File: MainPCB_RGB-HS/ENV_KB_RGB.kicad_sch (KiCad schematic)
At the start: 408 parts

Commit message: moved power input for mcu to vsys and also tweaked a bunch of traces to look nicer
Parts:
- C1, C10, C100, C101, C102, C11, C12, C13, C14, C15, C16, C17, C18, C19, C2, C20, C21, C22, C23, C24, C25, C26, C27, C28, C29, C3, C30, C31, C32, C33, C34, C35, C36, C37, C38, C39, C4, C40, C41, C42, C43, C44, C45, C46, C47, C48, C49, C5, C50, C51, C52, C53, C54, C55, C56, C57, C58, C59, C6, C60, C61, C62, C63, C64, C65, C66, C67, C68, C69, C7, C70, C71, C72, C73, C74, C75, C76, C77, C78, C79, C8, C80, C81, C82, C83, C84, C85, C86, C87, C88, C89, C9, C90, C91, C92, C93, C94, C95, C96, C97, C98, C99: value (none) -> 100nF 0603; footprint (none) -> Capacitor_SMD:C_0603_1608Metric
- D0, D1, D10, D11, D12, D13, D14, D15, D16, D17, D18, D19, D2, D20, D21, D22, D23, D24, D25, D26, D27, D28, D29, D3, D30, D31, D32, D33, D34, D35, D36, D37, D38, D39, D4, D40, D41, D42, D43, D44, D45, D46, D47, D48, D49, D5, D50, D51, D52, D53, D54, D55, D56, D57, D58, D59, D6, D60, D61, D62, D63, D64, D65, D66, D67, D68, D69, D7, D70, D71, D72, D73, D74, D75, D76, D77, D78, D79, D8, D80, D81, D82, D83, D84, D85, D86, D87, D88, D9: value (none) -> D; footprint (none) -> EM_Extras:SOD-123+D_DO-35_SOD27_P7.62mm_Horizontal
- H0, H1, H10, H2, H3, H4, H5, H6, H7, H9: value (none) -> MountingHole; footprint (none) -> MountingHole:MountingHole_2.2mm_M2_Pad
- K_0, K_1, K_10, K_11, K_12, K_13, K_14, K_15, K_16, K_17, K_18, K_19, K_2, K_20, K_21, K_22, K_23, K_24, K_25, K_26, K_27, K_28, K_29, K_3, K_30, K_31, K_32, K_33, K_34, K_35, K_36, K_37, K_38, K_39, K_4, K_40, K_41, K_42, K_43, K_44, K_45, K_46, K_47, K_48, K_49, K_5, K_50, K_51, K_52, K_53, K_54, K_55, K_56, K_57, K_58, K_59, K_6, K_60, K_61, K_62, K_63, K_63B1, K_64, K_64B1, K_65, K_66, K_67, K_68, K_69, K_7, K_70, K_71, K_72, K_73, K_74, K_75, K_76, K_77, K_78, K_79, K_8, K_80, K_81, K_82, K_83, K_84, K_85, K_86, K_87, K_88, K_9: value (none) -> KEYSW; footprint (none) -> MX_Only:MXOnly-1U-Hotswap-Modified
- LED1, LED10, LED100, LED101, LED102, LED11, LED12, LED13, LED14, LED15, LED16, LED17, LED18, LED19, LED2, LED20, LED21, LED22, LED23, LED24, LED25, LED26, LED27, LED28, LED29, LED3, LED30, LED31, LED32, LED33, LED34, LED35, LED36, LED37, LED38, LED39, LED4, LED40, LED41, LED42, LED43, LED44, LED45, LED46, LED47, LED48, LED49, LED5, LED50, LED51, LED52, LED53, LED54, LED55, LED56, LED57, LED58, LED59, LED6, LED60, LED61, LED62, LED63, LED64, LED65, LED66, LED67, LED68, LED69, LED7, LED70, LED71, LED72, LED73, LED74, LED75, LED76, LED77, LED78, LED79, LED8, LED80, LED81, LED82, LED83, LED84, LED85, LED86, LED87, LED88, LED89, LED9, LED90, LED91, LED92, LED93, LED94, LED95, LED96, LED97, LED98, LED99: value (none) -> SK6812MINI-E; footprint (none) -> sk6812mini:MX_SK6812MINI-E_REV
- LEDRESISTOR1: value (none) -> 5.1K Resistor 1/4w; footprint (none) -> Resistor_THT:R_Axial_DIN0207_L6.3mm_D2.5mm_P10.16mm_Horizontal
- LEDRESISTOR2: value (none) -> 5.1K Resistor 1/4w; footprint (none) -> Resistor_SMD:R_0805_2012Metric_Pad1.20x1.40mm_HandSolder
- PowerLED0: value (none) -> LED 3MM; footprint (none) -> LED_THT:LED_D3.0mm_FlatTop
- RESISTOR0: value (none) -> 5.1kohm 1/4w; footprint (none) -> Resistor_THT:R_Axial_DIN0207_L6.3mm_D2.5mm_P10.16mm_Horizontal
- RESISTOR1: value (none) -> 5.1kohm 1/4; footprint (none) -> Resistor_THT:R_Axial_DIN0207_L6.3mm_D2.5mm_P10.16mm_Horizontal
- RESISTOR2, RESISTOR3: value (none) -> 5.1kohm 0805; footprint (none) -> Resistor_SMD:R_0805_2012Metric
- RPI0: value (none) -> Pico; footprint (none) -> EM_Extras:RPi_Pico_SMD_TH
- SW-RST0: value (none) -> EVQ; footprint (none) -> Button_Switch_SMD:Panasonic_EVQPUM_EVQPUD
- Stab1: value (none) -> Stabilizer; footprint (none) -> Mounting_Keyboard_Stabilizer:Stabilizer_Cherry_MX_6.25u
- Stab2, Stab3, Stab4: value (none) -> Stabilizer; footprint (none) -> Mounting_Keyboard_Stabilizer:Stabilizer_Cherry_MX_2u
- USB1: value (none) -> TYPE-C-31-M-14; footprint (none) -> josh-connectors:USB_C_TYPE-C-31-M-14
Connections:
- net USBVBUS: now also RPI0.39 (VSYS); no longer RPI0.40 (VBUS)

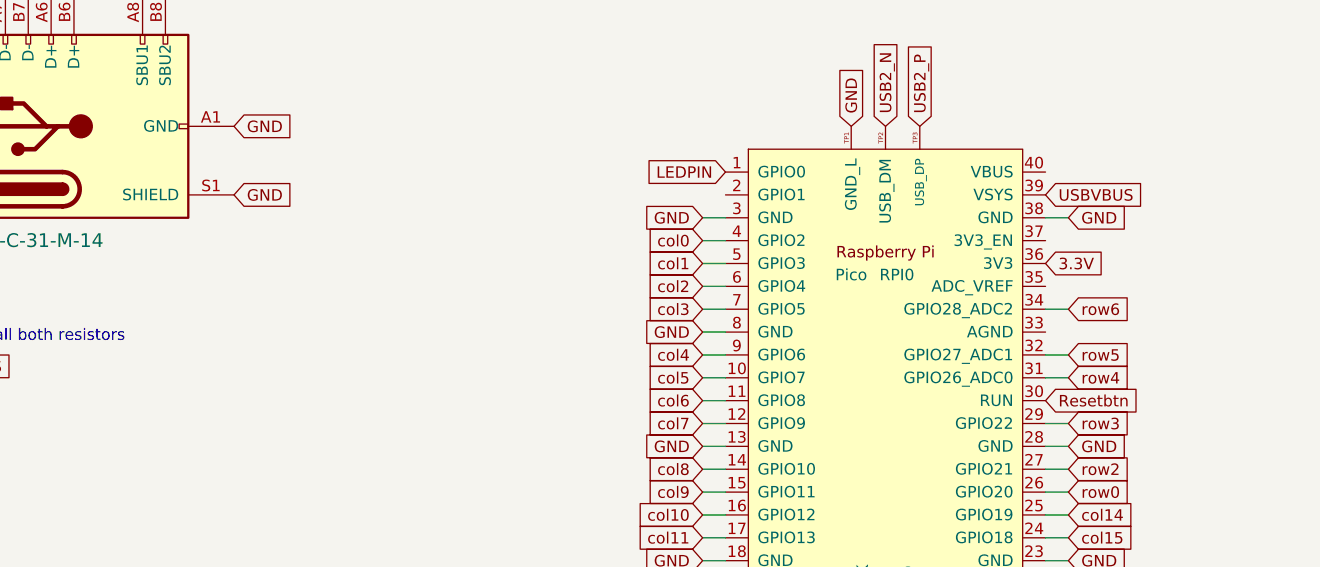
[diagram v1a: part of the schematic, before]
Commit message: Parity changes between RGB and non RGB HS versions
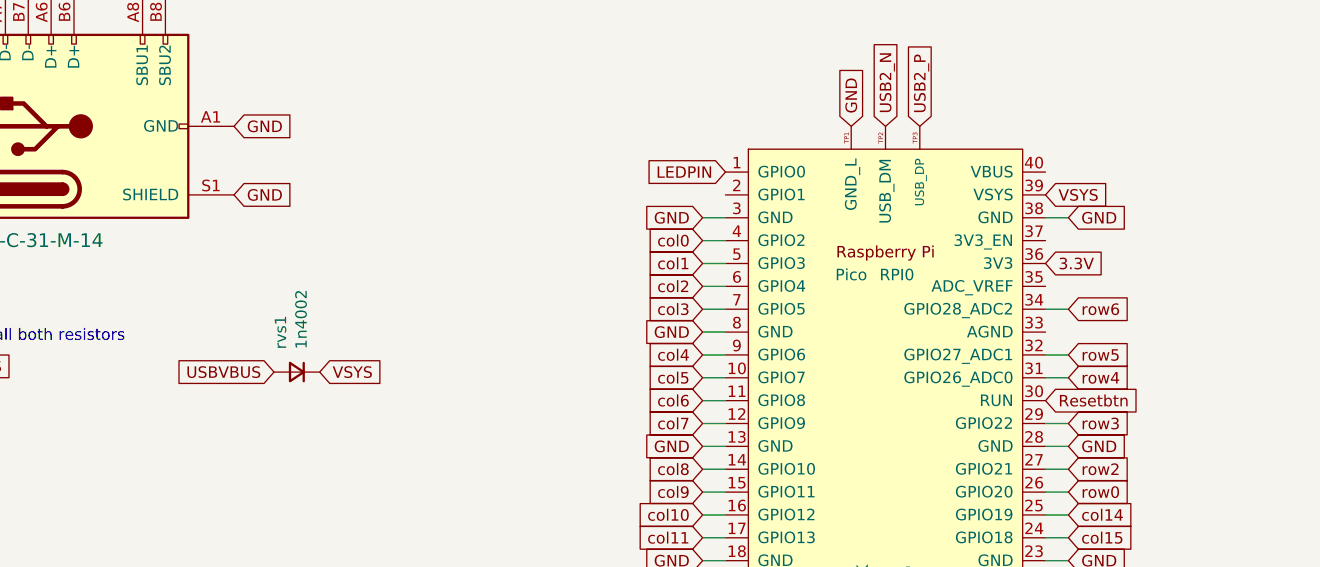
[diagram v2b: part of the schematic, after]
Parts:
- added rvs1: 1n4002, EM_Extras:SOD-123+D_DO-35_SOD27_P7.62mm_Horizontal, symbol Device:D_Small
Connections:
- net USBVBUS: now also rvs1.2 (A); no longer RPI0.39 (VSYS)
- new net VSYS: RPI0.39 (VSYS), rvs1.1 (K)
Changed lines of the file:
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@@
     )
   )
-  (global_label "USBVBUS" (shape input) (at 346.71 233.68 0) (fields_autoplaced)
-    (effects (font (size 1.27 1.27)) (justify left))
-    (property "Intersheet References" "${INTERSHEET_REFS}" (id 0) (at 0 2.54 0)
+  (global_label "USBVBUS" (shape input) (at 260.985 253.365 180) (fields_autoplaced)
+    (effects (font (size 1.27 1.27)) (justify right))
+    (property "Intersheet References" "${INTERSHEET_REFS}" (id 0) (at 607.695 484.505 0)
       (effects (font (size 1.27 1.27)) hide)
     )
@@
     )
   )
+  (global_label "VSYS" (shape input) (at 266.065 253.365 0) (fields_autoplaced)
+    (effects (font (size 1.27 1.27)) (justify left))
+    (property "Intersheet References" "${INTERSHEET_REFS}" (id 0) (at 272.9854 253.2856 0)
+      (effects (font (size 1.27 1.27)) (justify left) hide)
+    )
+  )
   (global_label "col14" (shape input) (at 349.25 269.24 0) (fields_autoplaced)
     (effects (font (size 1.27 1.27)) (justify left))
@@
     )
   )
+  (global_label "VSYS" (shape input) (at 346.71 233.68 0) (fields_autoplaced)
+    (effects (font (size 1.27 1.27)) (justify left))
+    (property "Intersheet References" "${INTERSHEET_REFS}" (id 0) (at 353.6304 233.6006 0)
+      (effects (font (size 1.27 1.27)) (justify left) hide)
+    )
+  )
   (global_label "USBVBUS" (shape input) (at 553.72 102.87 180) (fields_autoplaced)
     (effects (font (size 1.27 1.27)) (justify right))
@@
     (pin "2")
   )
+  (symbol (lib_id "Device:D_Small") (at 263.525 253.365 180) (unit 1)
+    (in_bom yes) (on_board yes)
+    (property "Reference" "rvs1" (id 0) (at 261.747 250.825 90)
+      (effects (font (size 1.27 1.27)) (justify right))
+    )
+    (property "Value" "1n4002" (id 1) (at 264.033 250.825 90)
+      (effects (font (size 1.27 1.27)) (justify right))
+    )
+    (property "Footprint" "EM_Extras:SOD-123+D_DO-35_SOD27_P7.62mm_Horizontal" (id 2) (at 271.145 252.095 0)
+      (effects (font (size 1.27 1.27)) hide)
+    )
+    (property "Datasheet" "" (id 3) (at 271.145 252.095 0)
+      (effects (font (size 1.27 1.27)) hide)
+    )
+    (pin "1")
+    (pin "2")
+  )
   (sheet_instances
     (path "/" (page "1"))
@@
       (reference "USB1") (unit 1) (value "TYPE-C-31-M-14") (footprint "josh-connectors:USB_C_TYPE-C-31-M-14")
     )
+    (path "/fe72a08a-d529-4860-95f3-bd42d36f7bb1"
+      (reference "rvs1") (unit 1) (value "1n4002") (footprint "EM_Extras:SOD-123+D_DO-35_SOD27_P7.62mm_Horizontal")
+    )
   )

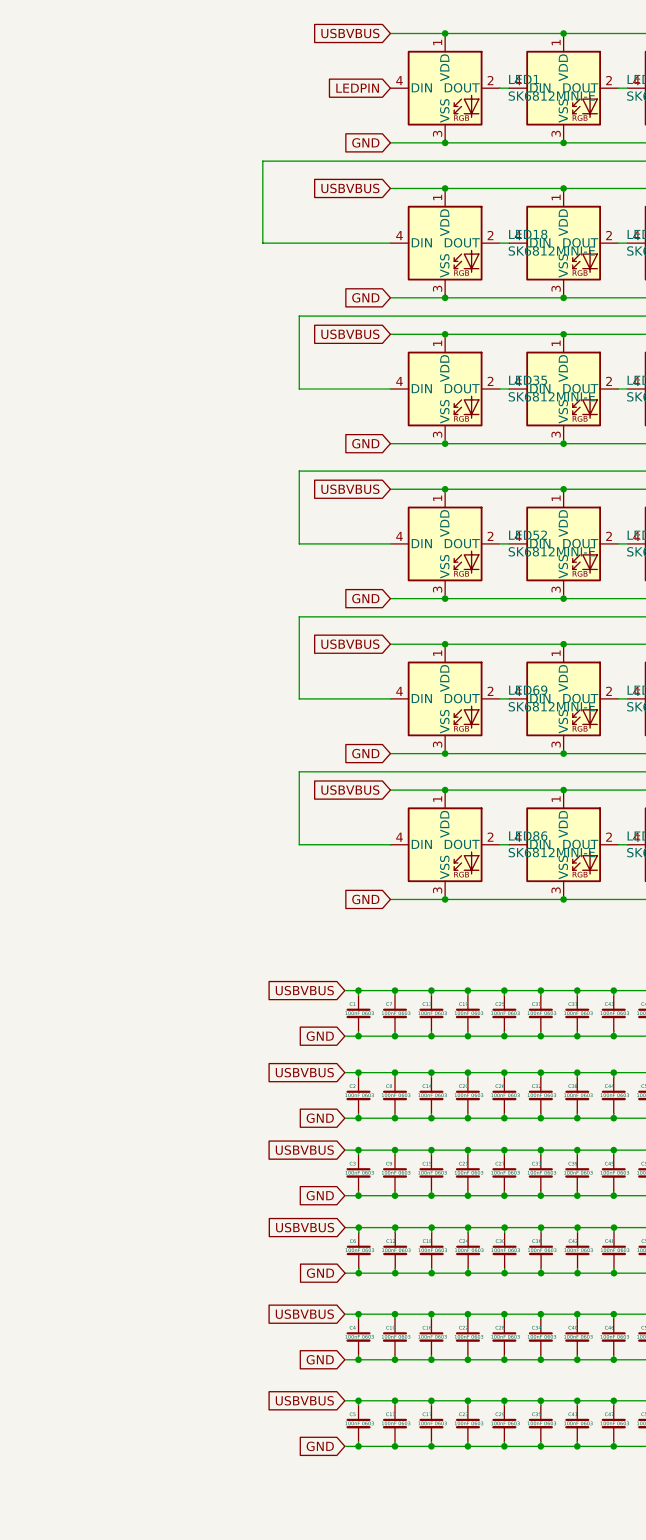
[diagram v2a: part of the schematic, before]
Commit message: Swapped VBUS power to VSYS and fixed edge cut issues.
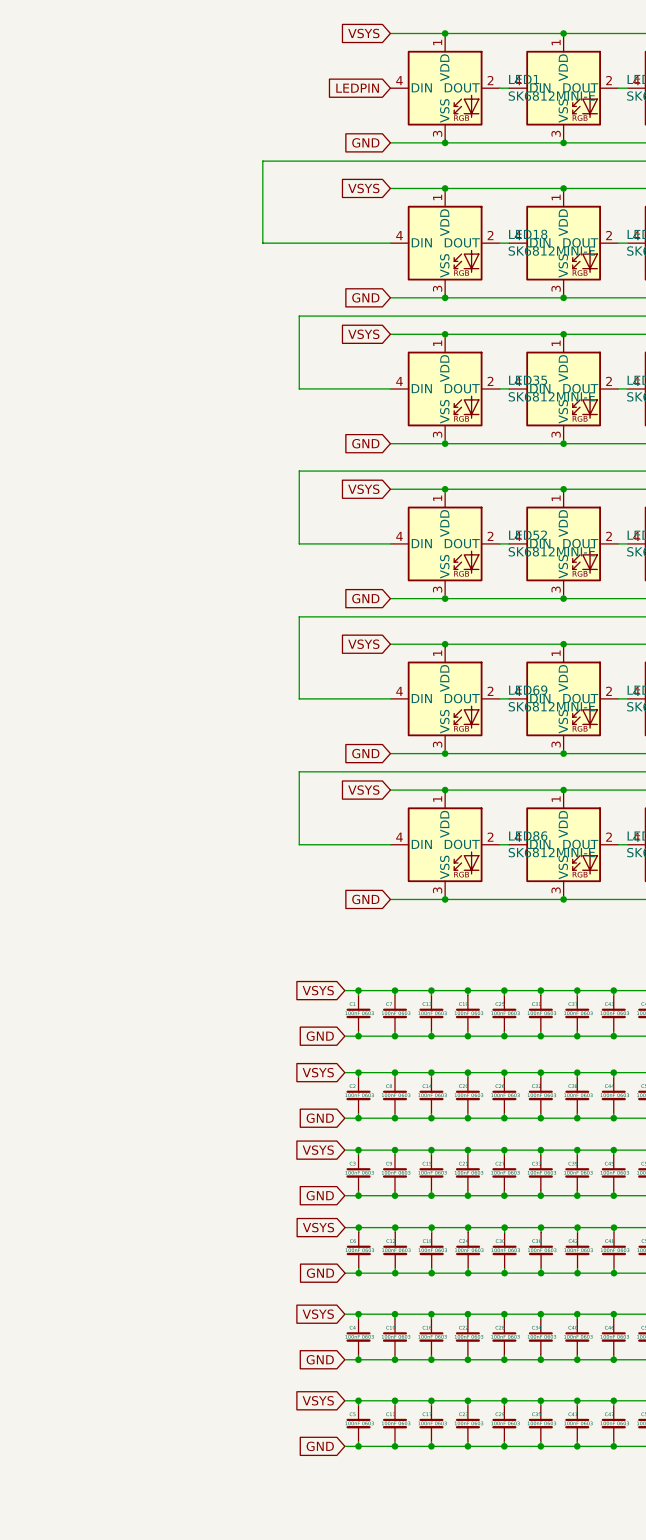
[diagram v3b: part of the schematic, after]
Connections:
- net USBVBUS: no longer C1.1, C10.1, C100.1, C101.1, C102.1, C11.1, C12.1, C13.1, C14.1, C15.1, C16.1, C17.1, C18.1, C19.1, C2.1, C20.1, C21.1, C22.1, C23.1, C24.1, C25.1, C26.1, C27.1, C28.1, C29.1, C3.1, C30.1, C31.1, C32.1, C33.1, C34.1, C35.1, C36.1, C37.1, C38.1, C39.1, C4.1, C40.1, C41.1, C42.1, C43.1, C44.1, C45.1, C46.1, C47.1, C48.1, C49.1, C5.1, C50.1, C51.1, C52.1, C53.1, C54.1, C55.1, C56.1, C57.1, C58.1, C59.1, C6.1, C60.1, C61.1, C62.1, C63.1, C64.1, C65.1, C66.1, C67.1, C68.1, C69.1, C7.1, C70.1, C71.1, C72.1, C73.1, C74.1, C75.1, C76.1, C77.1, C78.1, C79.1, C8.1, C80.1, C81.1, C82.1, C83.1, C84.1, C85.1, C86.1, C87.1, C88.1, C89.1, C9.1, C90.1, C91.1, C92.1, C93.1, C94.1, C95.1, C96.1, C97.1, C98.1, C99.1, LED1.1 (VDD), LED10.1 (VDD), LED100.1 (VDD), LED101.1 (VDD), LED102.1 (VDD), LED11.1 (VDD), LED12.1 (VDD), LED13.1 (VDD), LED14.1 (VDD), LED15.1 (VDD), LED16.1 (VDD), LED17.1 (VDD), LED18.1 (VDD), LED19.1 (VDD), LED2.1 (VDD), LED20.1 (VDD), LED21.1 (VDD), LED22.1 (VDD), LED23.1 (VDD), LED24.1 (VDD), LED25.1 (VDD), LED26.1 (VDD), LED27.1 (VDD), LED28.1 (VDD), LED29.1 (VDD), LED3.1 (VDD), LED30.1 (VDD), LED31.1 (VDD), LED32.1 (VDD), LED33.1 (VDD), LED34.1 (VDD), LED35.1 (VDD), LED36.1 (VDD), LED37.1 (VDD), LED38.1 (VDD), LED39.1 (VDD), LED4.1 (VDD), LED40.1 (VDD), LED41.1 (VDD), LED42.1 (VDD), LED43.1 (VDD), LED44.1 (VDD), LED45.1 (VDD), LED46.1 (VDD), LED47.1 (VDD), LED48.1 (VDD), LED49.1 (VDD), LED5.1 (VDD), LED50.1 (VDD), LED51.1 (VDD), LED52.1 (VDD), LED53.1 (VDD), LED54.1 (VDD), LED55.1 (VDD), LED56.1 (VDD), LED57.1 (VDD), LED58.1 (VDD), LED59.1 (VDD), LED6.1 (VDD), LED60.1 (VDD), LED61.1 (VDD), LED62.1 (VDD), LED63.1 (VDD), LED64.1 (VDD), LED65.1 (VDD), LED66.1 (VDD), LED67.1 (VDD), LED68.1 (VDD), LED69.1 (VDD), LED7.1 (VDD), LED70.1 (VDD), LED71.1 (VDD), LED72.1 (VDD), LED73.1 (VDD), LED74.1 (VDD), LED75.1 (VDD), LED76.1 (VDD), LED77.1 (VDD), LED78.1 (VDD), LED79.1 (VDD), LED8.1 (VDD), LED80.1 (VDD), LED81.1 (VDD), LED82.1 (VDD), LED83.1 (VDD), LED84.1 (VDD), LED85.1 (VDD), LED86.1 (VDD), LED87.1 (VDD), LED88.1 (VDD), LED89.1 (VDD), LED9.1 (VDD), LED90.1 (VDD), LED91.1 (VDD), LED92.1 (VDD), LED93.1 (VDD), LED94.1 (VDD), LED95.1 (VDD), LED96.1 (VDD), LED97.1 (VDD), LED98.1 (VDD), LED99.1 (VDD)
- net VSYS: now also C1.1, C10.1, C100.1, C101.1, C102.1, C11.1, C12.1, C13.1, C14.1, C15.1, C16.1, C17.1, C18.1, C19.1, C2.1, C20.1, C21.1, C22.1, C23.1, C24.1, C25.1, C26.1, C27.1, C28.1, C29.1, C3.1, C30.1, C31.1, C32.1, C33.1, C34.1, C35.1, C36.1, C37.1, C38.1, C39.1, C4.1, C40.1, C41.1, C42.1, C43.1, C44.1, C45.1, C46.1, C47.1, C48.1, C49.1, C5.1, C50.1, C51.1, C52.1, C53.1, C54.1, C55.1, C56.1, C57.1, C58.1, C59.1, C6.1, C60.1, C61.1, C62.1, C63.1, C64.1, C65.1, C66.1, C67.1, C68.1, C69.1, C7.1, C70.1, C71.1, C72.1, C73.1, C74.1, C75.1, C76.1, C77.1, C78.1, C79.1, C8.1, C80.1, C81.1, C82.1, C83.1, C84.1, C85.1, C86.1, C87.1, C88.1, C89.1, C9.1, C90.1, C91.1, C92.1, C93.1, C94.1, C95.1, C96.1, C97.1, C98.1, C99.1, LED1.1 (VDD), LED10.1 (VDD), LED100.1 (VDD), LED101.1 (VDD), LED102.1 (VDD), LED11.1 (VDD), LED12.1 (VDD), LED13.1 (VDD), LED14.1 (VDD), LED15.1 (VDD), LED16.1 (VDD), LED17.1 (VDD), LED18.1 (VDD), LED19.1 (VDD), LED2.1 (VDD), LED20.1 (VDD), LED21.1 (VDD), LED22.1 (VDD), LED23.1 (VDD), LED24.1 (VDD), LED25.1 (VDD), LED26.1 (VDD), LED27.1 (VDD), LED28.1 (VDD), LED29.1 (VDD), LED3.1 (VDD), LED30.1 (VDD), LED31.1 (VDD), LED32.1 (VDD), LED33.1 (VDD), LED34.1 (VDD), LED35.1 (VDD), LED36.1 (VDD), LED37.1 (VDD), LED38.1 (VDD), LED39.1 (VDD), LED4.1 (VDD), LED40.1 (VDD), LED41.1 (VDD), LED42.1 (VDD), LED43.1 (VDD), LED44.1 (VDD), LED45.1 (VDD), LED46.1 (VDD), LED47.1 (VDD), LED48.1 (VDD), LED49.1 (VDD), LED5.1 (VDD), LED50.1 (VDD), LED51.1 (VDD), LED52.1 (VDD), LED53.1 (VDD), LED54.1 (VDD), LED55.1 (VDD), LED56.1 (VDD), LED57.1 (VDD), LED58.1 (VDD), LED59.1 (VDD), LED6.1 (VDD), LED60.1 (VDD), LED61.1 (VDD), LED62.1 (VDD), LED63.1 (VDD), LED64.1 (VDD), LED65.1 (VDD), LED66.1 (VDD), LED67.1 (VDD), LED68.1 (VDD), LED69.1 (VDD), LED7.1 (VDD), LED70.1 (VDD), LED71.1 (VDD), LED72.1 (VDD), LED73.1 (VDD), LED74.1 (VDD), LED75.1 (VDD), LED76.1 (VDD), LED77.1 (VDD), LED78.1 (VDD), LED79.1 (VDD), LED8.1 (VDD), LED80.1 (VDD), LED81.1 (VDD), LED82.1 (VDD), LED83.1 (VDD), LED84.1 (VDD), LED85.1 (VDD), LED86.1 (VDD), LED87.1 (VDD), LED88.1 (VDD), LED89.1 (VDD), LED9.1 (VDD), LED90.1 (VDD), LED91.1 (VDD), LED92.1 (VDD), LED93.1 (VDD), LED94.1 (VDD), LED95.1 (VDD), LED96.1 (VDD), LED97.1 (VDD), LED98.1 (VDD), LED99.1 (VDD)
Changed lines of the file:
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@@
     (effects (font (size 1.27 1.27)) (justify left bottom))
   )
+  (global_label "VSYS" (shape input) (at 547.4032 184.15 180) (fields_autoplaced)
+    (effects (font (size 1.27 1.27)) (justify right))
+    (property "Intersheet References" "${INTERSHEET_REFS}" (id 0) (at 540.4828 184.2294 0)
+      (effects (font (size 1.27 1.27)) (justify right) hide)
+    )
+  )
   (global_label "row0" (shape input) (at 349.25 266.7 0) (fields_autoplaced)
     (effects (font (size 1.27 1.27)) (justify left))
@@
     )
   )
+  (global_label "VSYS" (shape input) (at 553.72 39.37 180) (fields_autoplaced)
+    (effects (font (size 1.27 1.27)) (justify right))
+    (property "Intersheet References" "${INTERSHEET_REFS}" (id 0) (at 546.7996 39.4494 0)
+      (effects (font (size 1.27 1.27)) (justify right) hide)
+    )
+  )
+  (global_label "VSYS" (shape input) (at 553.72 81.28 180) (fields_autoplaced)
+    (effects (font (size 1.27 1.27)) (justify right))
+    (property "Intersheet References" "${INTERSHEET_REFS}" (id 0) (at 546.7996 81.3594 0)
+      (effects (font (size 1.27 1.27)) (justify right) hide)
+    )
+  )
   (global_label "USB2_N" (shape input) (at 328.93 226.06 90) (fields_autoplaced)
     (effects (font (size 1.27 1.27)) (justify left))
@@
     )
   )
+  (global_label "VSYS" (shape input) (at 553.72 123.19 180) (fields_autoplaced)
+    (effects (font (size 1.27 1.27)) (justify right))
+    (property "Intersheet References" "${INTERSHEET_REFS}" (id 0) (at 546.7996 123.2694 0)
+      (effects (font (size 1.27 1.27)) (justify right) hide)
+    )
+  )
   (global_label "row4" (shape input) (at 22.86 137.16 180) (fields_autoplaced)
     (effects (font (size 1.27 1.27)) (justify right))
@@
     )
   )
+  (global_label "VSYS" (shape input) (at 553.72 59.69 180) (fields_autoplaced)
+    (effects (font (size 1.27 1.27)) (justify right))
+    (property "Intersheet References" "${INTERSHEET_REFS}" (id 0) (at 546.7996 59.7694 0)
+      (effects (font (size 1.27 1.27)) (justify right) hide)
+    )
+  )
   (global_label "GND" (shape input) (at 547.37 202.565 180) (fields_autoplaced)
     (effects (font (size 1.27 1.27)) (justify right))
@@
     )
   )
-  (global_label "USBVBUS" (shape input) (at 547.37 208.28 180) (fields_autoplaced)
-    (effects (font (size 1.27 1.27)) (justify right))
-    (property "Intersheet References" "${INTERSHEET_REFS}" (id 0) (at -6.35 190.5 0)
-      (effects (font (size 1.27 1.27)) hide)
+  (global_label "VSYS" (shape input) (at 553.72 17.78 180) (fields_autoplaced)
+    (effects (font (size 1.27 1.27)) (justify right))
+    (property "Intersheet References" "${INTERSHEET_REFS}" (id 0) (at 546.7996 17.8594 0)
+      (effects (font (size 1.27 1.27)) (justify right) hide)
     )
   )
@@
     )
   )
-  (global_label "USBVBUS" (shape input) (at 553.72 123.19 180) (fields_autoplaced)
-    (effects (font (size 1.27 1.27)) (justify right))
-    (property "Intersheet References" "${INTERSHEET_REFS}" (id 0) (at 0 0 0)
-      (effects (font (size 1.27 1.27)) hide)
-    )
-  )
   (global_label "GND" (shape input) (at 553.72 54.61 180) (fields_autoplaced)
     (effects (font (size 1.27 1.27)) (justify right))
@@
     )
   )
-  (global_label "USBVBUS" (shape input) (at 547.37 173.355 180) (fields_autoplaced)
-    (effects (font (size 1.27 1.27)) (justify right))
-    (property "Intersheet References" "${INTERSHEET_REFS}" (id 0) (at -6.35 155.575 0)
-      (effects (font (size 1.27 1.27)) hide)
-    )
-  )
-  (global_label "USBVBUS" (shape input) (at 553.72 39.37 180) (fields_autoplaced)
-    (effects (font (size 1.27 1.27)) (justify right))
-    (property "Intersheet References" "${INTERSHEET_REFS}" (id 0) (at 0 0 0)
-      (effects (font (size 1.27 1.27)) hide)
-    )
-  )
   (global_label "GND" (shape input) (at 223.52 193.675 90) (fields_autoplaced)
     (effects (font (size 1.27 1.27)) (justify left))
@@
     )
   )
-  (global_label "USBVBUS" (shape input) (at 553.72 59.69 180) (fields_autoplaced)
-    (effects (font (size 1.27 1.27)) (justify right))
-    (property "Intersheet References" "${INTERSHEET_REFS}" (id 0) (at 0 0 0)
-      (effects (font (size 1.27 1.27)) hide)
-    )
-  )
   (global_label "col7" (shape input) (at 223.52 16.51 180) (fields_autoplaced)
     (effects (font (size 1.27 1.27)) (justify right))
@@
     )
   )
-  (global_label "USBVBUS" (shape input) (at 553.72 17.78 180) (fields_autoplaced)
-    (effects (font (size 1.27 1.27)) (justify right))
-    (property "Intersheet References" "${INTERSHEET_REFS}" (id 0) (at 0 0 0)
-      (effects (font (size 1.27 1.27)) hide)
-    )
-  )
   (global_label "GND" (shape input) (at 553.72 33.02 180) (fields_autoplaced)
     (effects (font (size 1.27 1.27)) (justify right))
@@
     )
   )
-  (global_label "USBVBUS" (shape input) (at 547.37 162.56 180) (fields_autoplaced)
-    (effects (font (size 1.27 1.27)) (justify right))
-    (property "Intersheet References" "${INTERSHEET_REFS}" (id 0) (at -6.35 144.78 0)
-      (effects (font (size 1.27 1.27)) hide)
-    )
-  )
-  (global_label "USBVBUS" (shape input) (at 547.37 151.13 180) (fields_autoplaced)
-    (effects (font (size 1.27 1.27)) (justify right))
-    (property "Intersheet References" "${INTERSHEET_REFS}" (id 0) (at -6.35 133.35 0)
-      (effects (font (size 1.27 1.27)) hide)
-    )
-  )
   (global_label "row3" (shape input) (at 22.86 111.76 180) (fields_autoplaced)
     (effects (font (size 1.27 1.27)) (justify right))
@@
     )
   )
-  (global_label "USBVBUS" (shape input) (at 547.4032 184.15 180) (fields_autoplaced)
-    (effects (font (size 1.27 1.27)) (justify right))
-    (property "Intersheet References" "${INTERSHEET_REFS}" (id 0) (at -6.3168 166.37 0)
-      (effects (font (size 1.27 1.27)) hide)
+  (global_label "VSYS" (shape input) (at 547.37 151.13 180) (fields_autoplaced)
+    (effects (font (size 1.27 1.27)) (justify right))
+    (property "Intersheet References" "${INTERSHEET_REFS}" (id 0) (at 540.4496 151.2094 0)
+      (effects (font (size 1.27 1.27)) (justify right) hide)
     )
   )
@@
     )
   )
-  (global_label "USBVBUS" (shape input) (at 547.37 196.215 180) (fields_autoplaced)
-    (effects (font (size 1.27 1.27)) (justify right))
-    (property "Intersheet References" "${INTERSHEET_REFS}" (id 0) (at -6.35 178.435 0)
-      (effects (font (size 1.27 1.27)) hide)
-    )
-  )
   (global_label "col7" (shape input) (at 308.61 259.08 180) (fields_autoplaced)
     (effects (font (size 1.27 1.27)) (justify right))
@@
     )
   )
+  (global_label "VSYS" (shape input) (at 547.37 196.215 180) (fields_autoplaced)
+    (effects (font (size 1.27 1.27)) (justify right))
+    (property "Intersheet References" "${INTERSHEET_REFS}" (id 0) (at 540.4496 196.2944 0)
+      (effects (font (size 1.27 1.27)) (justify right) hide)
+    )
+  )
   (global_label "USB2_N" (shape input) (at 231.14 210.82 90) (fields_autoplaced)
     (effects (font (size 1.27 1.27)) (justify left))
@@
     (property "Intersheet References" "${INTERSHEET_REFS}" (id 0) (at 0 0 0)
       (effects (font (size 1.27 1.27)) hide)
+    )
+  )
+  (global_label "VSYS" (shape input) (at 547.37 208.28 180) (fields_autoplaced)
+    (effects (font (size 1.27 1.27)) (justify right))
+    (property "Intersheet References" "${INTERSHEET_REFS}" (id 0) (at 540.4496 208.3594 0)
+      (effects (font (size 1.27 1.27)) (justify right) hide)
     )
   )
@@
     )
   )
-  (global_label "USBVBUS" (shape input) (at 553.72 81.28 180) (fields_autoplaced)
-    (effects (font (size 1.27 1.27)) (justify right))
-    (property "Intersheet References" "${INTERSHEET_REFS}" (id 0) (at 0 0 0)
-      (effects (font (size 1.27 1.27)) hide)
-    )
-  )
   (global_label "col1" (shape input) (at 308.61 241.3 180) (fields_autoplaced)
     (effects (font (size 1.27 1.27)) (justify right))
@@
     )
   )
+  (global_label "VSYS" (shape input) (at 547.37 173.355 180) (fields_autoplaced)
+    (effects (font (size 1.27 1.27)) (justify right))
+    (property "Intersheet References" "${INTERSHEET_REFS}" (id 0) (at 540.4496 173.4344 0)
+      (effects (font (size 1.27 1.27)) (justify right) hide)
+    )
+  )
   (global_label "GND" (shape input) (at 222.25 271.78 0) (fields_autoplaced)
     (effects (font (size 1.27 1.27)) (justify left))
@@
     )
   )
+  (global_label "VSYS" (shape input) (at 553.72 102.87 180) (fields_autoplaced)
+    (effects (font (size 1.27 1.27)) (justify right))
+    (property "Intersheet References" "${INTERSHEET_REFS}" (id 0) (at 546.7996 102.9494 0)
+      (effects (font (size 1.27 1.27)) (justify right) hide)
+    )
+  )
   (global_label "row3" (shape input) (at 349.25 259.08 0) (fields_autoplaced)
     (effects (font (size 1.27 1.27)) (justify left))
     (property "Intersheet References" "${INTERSHEET_REFS}" (id 0) (at 0 0 0)
       (effects (font (size 1.27 1.27)) hide)
+    )
+  )
+  (global_label "VSYS" (shape input) (at 547.37 162.56 180) (fields_autoplaced)
+    (effects (font (size 1.27 1.27)) (justify right))
+    (property "Intersheet References" "${INTERSHEET_REFS}" (id 0) (at 540.4496 162.6394 0)
+      (effects (font (size 1.27 1.27)) (justify right) hide)
     )
   )
@@
     )
   )
-  (global_label "USBVBUS" (shape input) (at 553.72 102.87 180) (fields_autoplaced)
-    (effects (font (size 1.27 1.27)) (justify right))
-    (property "Intersheet References" "${INTERSHEET_REFS}" (id 0) (at 0 0 0)
-      (effects (font (size 1.27 1.27)) hide)
-    )
-  )
